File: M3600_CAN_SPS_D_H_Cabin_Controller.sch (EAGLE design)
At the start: 7 parts

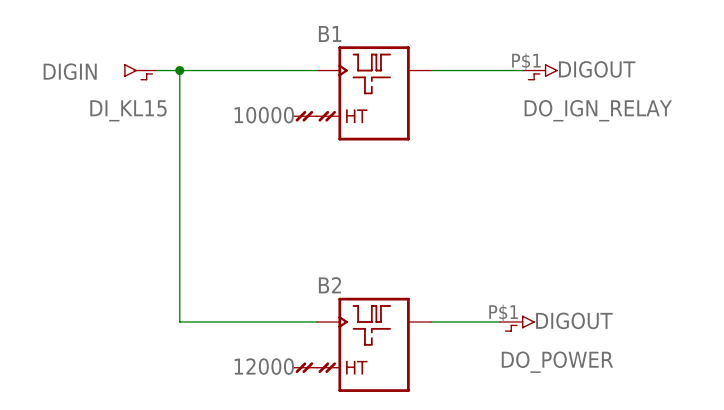
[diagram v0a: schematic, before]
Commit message: changed DO_IGN_RELAY to have no dela after, it is now used for power suply to "svirtele"
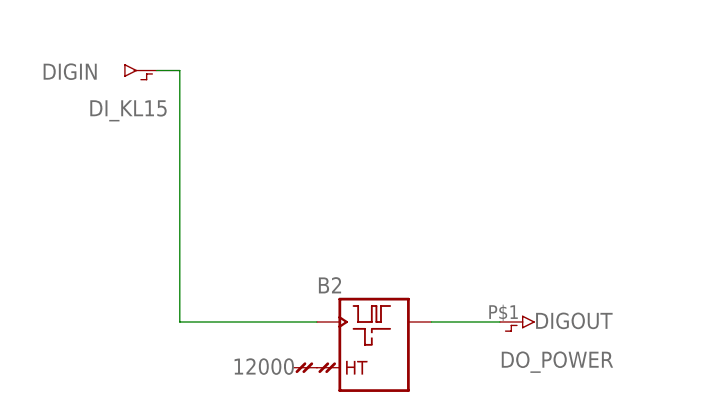
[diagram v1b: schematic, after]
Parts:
- removed B1: DELAY_OFF_RTR, CANgraph:DELAY_OFF_RTR
- removed DIGOUT1: DO_IGN_RELAY, CANgraph:DIGOUT
- removed VALUE#1: 10000, CANgraph:VALUE
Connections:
- removed net N$2: B1.2_32, VALUE#1.KONST_32
- removed net N$4: B1.3_1, DIGOUT1.AUS_1
- net N$1: no longer B1.1_1
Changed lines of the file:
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@@
 <part name="FRAME1" library="CANgraph" deviceset="CAN_FRAME" device=""/>
 <part name="DIGIN1" library="CANgraph" deviceset="DIGIN" device="" value="DI_KL15"/>
-<part name="B1" library="CANgraph" deviceset="DELAY_OFF_RTR" device=""/>
 <part name="B2" library="CANgraph" deviceset="DELAY_OFF_RTR" device=""/>
-<part name="DIGOUT1" library="CANgraph" deviceset="DIGOUT" device="" value="DO_IGN_RELAY"/>
 <part name="DIGOUT2" library="CANgraph" deviceset="DIGOUT" device="" value="DO_POWER"/>
-<part name="VALUE#1" library="CANgraph" deviceset="VALUE" device="" value="10000"/>
 <part name="VALUE#2" library="CANgraph" deviceset="VALUE" device="" value="12000"/>
 </parts>
@@
 <attribute name="VALUE" x="-254" y="93.98" size="1.778" layer="96" font="vector"/>
 </instance>
-<instance part="B1" gate="DELAY_OFF_RTR" x="-223.52" y="99.06" smashed="yes">
-<attribute name="NAME" x="-228.6" y="102.235" size="1.778" layer="95" font="vector"/>
-</instance>
 <instance part="B2" gate="DELAY_OFF_RTR" x="-223.52" y="71.12" smashed="yes">
 <attribute name="NAME" x="-228.6" y="74.295" size="1.778" layer="95" font="vector"/>
-</instance>
-<instance part="DIGOUT1" gate="DIGOUT" x="-200.66" y="99.06" smashed="yes">
-<attribute name="GATE" x="-201.93" y="98.298" size="1.778" layer="95" font="vector"/>
-<attribute name="VALUE" x="-205.74" y="93.98" size="1.778" layer="96" font="vector"/>
 </instance>
 <instance part="DIGOUT2" gate="DIGOUT" x="-203.2" y="71.12" smashed="yes">
 <attribute name="GATE" x="-204.47" y="70.358" size="1.778" layer="95" font="vector"/>
 <attribute name="VALUE" x="-208.28" y="66.04" size="1.778" layer="96" font="vector"/>
-</instance>
-<instance part="VALUE#1" gate="VALUE" x="-231.14" y="93.98" smashed="yes">
-<attribute name="VALUE" x="-231.013" y="94.996" size="1.778" layer="96" font="vector" rot="R180"/>
 </instance>
 <instance part="VALUE#2" gate="VALUE" x="-231.14" y="66.04" smashed="yes">
@@
 <segment>
 <pinref part="DIGIN1" gate="DIGIN" pin="EIN_1"/>
-<pinref part="B1" gate="DELAY_OFF_RTR" pin="1_1"/>
 <wire x1="-246.38" y1="99.06" x2="-243.84" y2="99.06" width="0.1524" layer="91"/>
 <pinref part="B2" gate="DELAY_OFF_RTR" pin="1_1"/>
-<wire x1="-243.84" y1="99.06" x2="-228.6" y2="99.06" width="0.1524" layer="91"/>
 <wire x1="-228.6" y1="71.12" x2="-243.84" y2="71.12" width="0.1524" layer="91"/>
 <wire x1="-243.84" y1="71.12" x2="-243.84" y2="99.06" width="0.1524" layer="91"/>
-<junction x="-243.84" y="99.06"/>
-</segment>
-</net>
-<net name="N$2" class="0">
-<segment>
-<pinref part="VALUE#1" gate="VALUE" pin="KONST_32"/>
-<pinref part="B1" gate="DELAY_OFF_RTR" pin="2_32"/>
 </segment>
 </net>
@@
 </segment>
 </net>
-<net name="N$4" class="0">
-<segment>
-<pinref part="B1" gate="DELAY_OFF_RTR" pin="3_1"/>
-<pinref part="DIGOUT1" gate="DIGOUT" pin="AUS_1"/>
-<wire x1="-215.9" y1="99.06" x2="-205.74" y2="99.06" width="0.1524" layer="91"/>
-</segment>
-</net>
